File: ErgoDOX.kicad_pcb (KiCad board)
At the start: 2 copper layers, 182.8 x 158.9 mm, 103 parts, among them J1 SPLIT_JACK_TOP, J1 USB, J2 3.5mm, J2 EXT1_TOP, J3 EXT1_BOT, J3 JMP, J4 EXT1_TOP2, J4 JMP, J5 SPLIT_JACK_BOT, J6 USB_C_TOP, J7 USB_C_BOT, SW0:10 SW0:3, SW0:11 SW0:2, SW0:12 SW0:1, SW0:7 SW0:6, SW0:8 SW0:5, SW0:9 SW0:4, SW1:10 SW1:3, SW1:11 SW1:2, SW1:12 SW1:1, SW1:13 SW1:0, SW1:9 SW1:4, SW2:10 SW2:3, SW2:11 SW2:2, SW2:12 SW2:1, SW2:13 SW2:0, SW2:7 SW2:6, SW2:8 SW2:5, SW2:9 SW2:4, SW3:10 SW3:3, SW3:11 SW3:2, SW3:12 SW3:1, SW3:13 SW3:0, SW3:8 SW3:5, SW3:9 SW3:4, SW4:10 SW4:3, SW4:11 SW4:2, SW4:12 SW4:1, SW4:13 SW4:0, SW4:7 SW4:6, SW4:8 SW4:5, SW4:9 SW4:4, SW5:10 SW5:3, SW5:11 SW5:2, SW5:12 SW5:1, SW5:13 SW5:0, SW5:7 SW5:6, SW5:8 SW5:5, SW5:9 SW5:4, U1 STM32F072C8Tx, U1 TEENSY2.0, U2 MCP1700-1202E_SOT23, U2 MCP23018

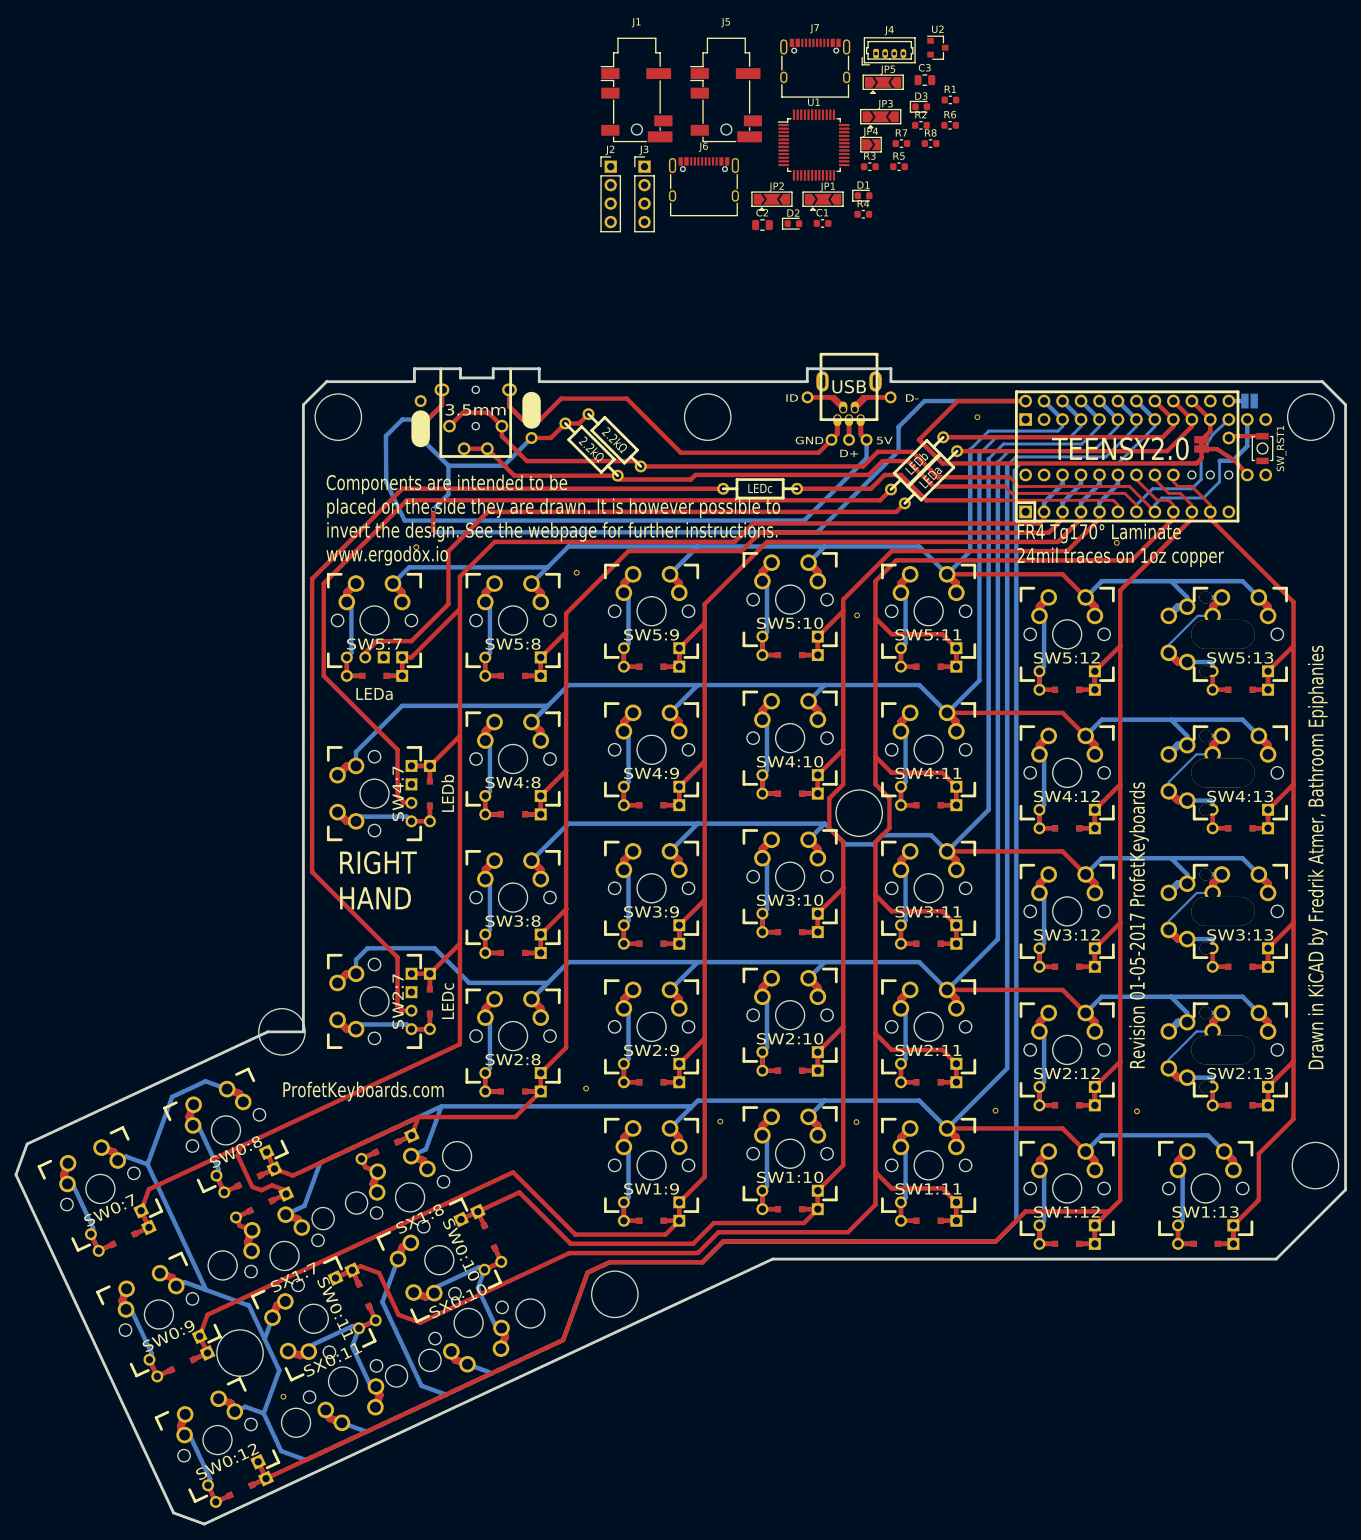
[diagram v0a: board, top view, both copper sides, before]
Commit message: Routing done, needs review.
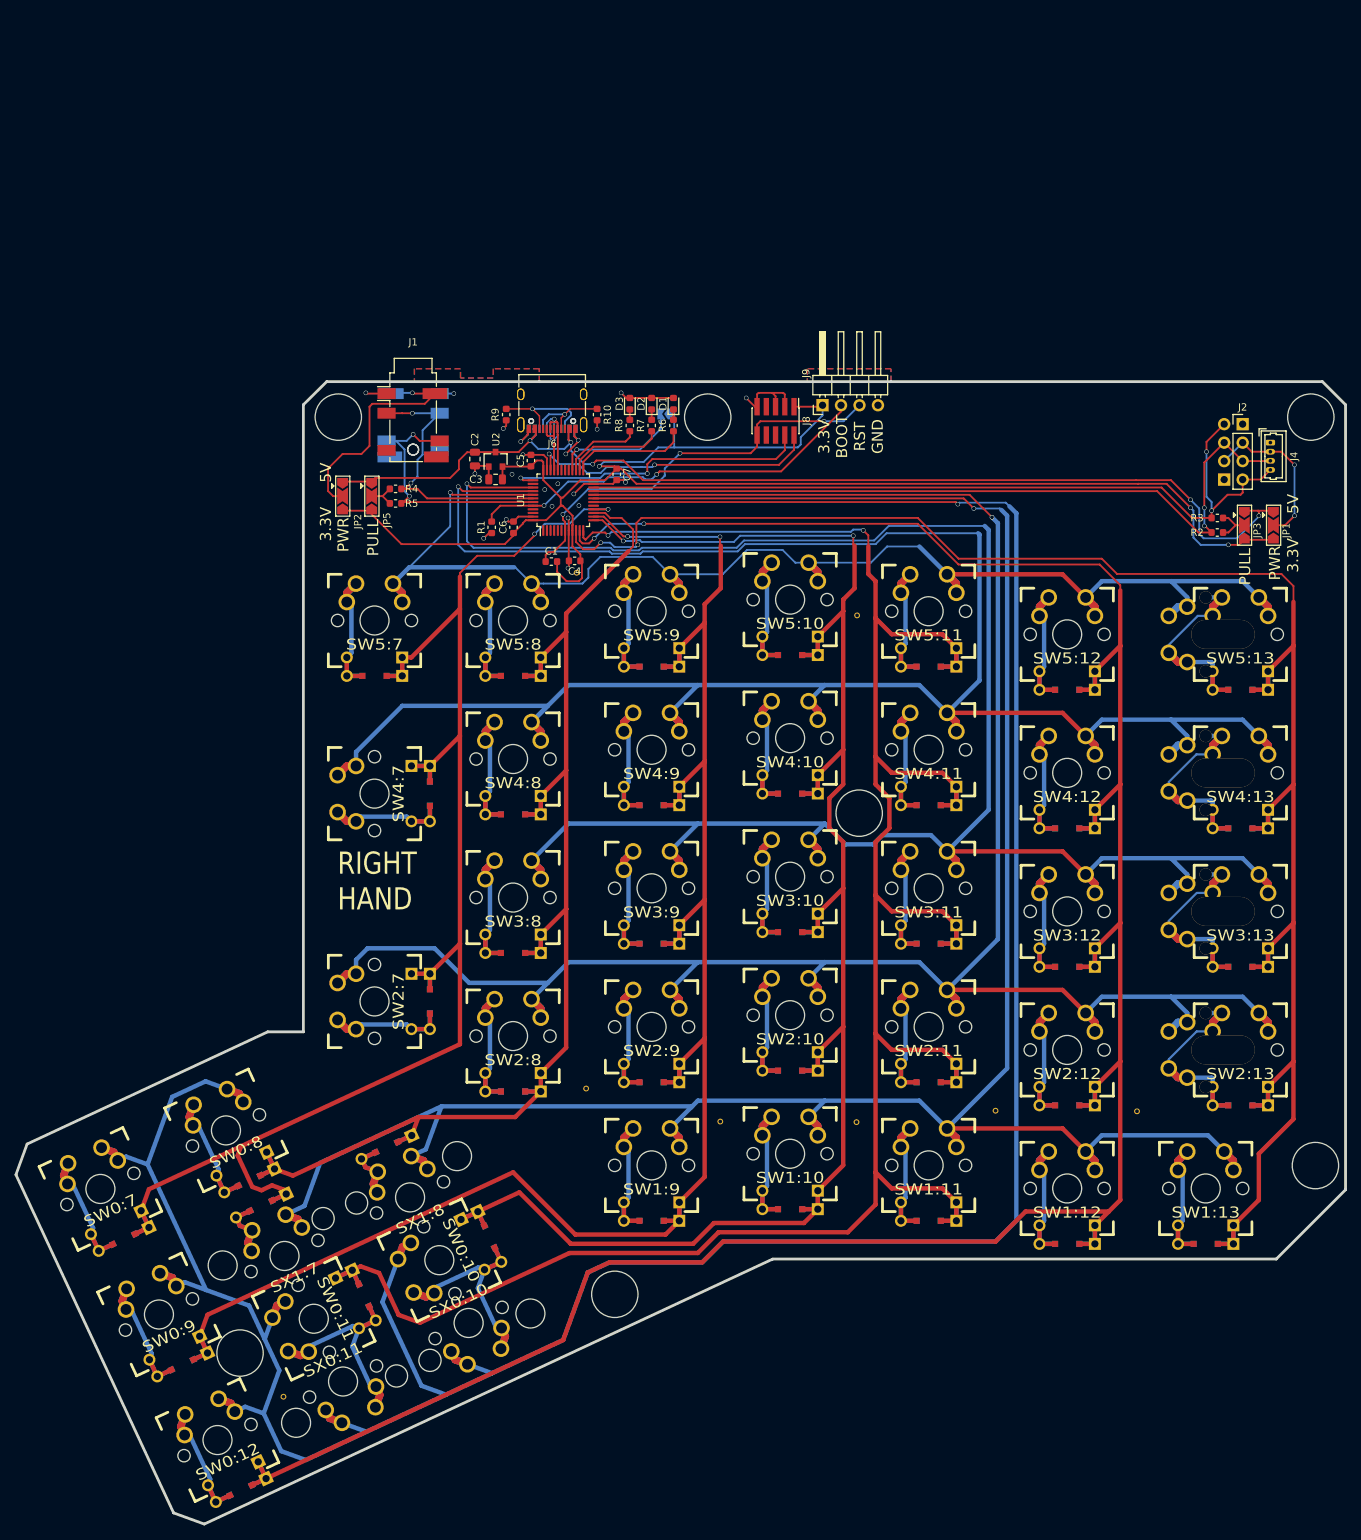
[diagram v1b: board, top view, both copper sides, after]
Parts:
- removed the J1 at (137.6, 30.5)
- removed the J2 at (86.3, 30.5)
- removed the J3 at (94.0, 37.5)
- removed the J4 at (78.7, 37.5)
- removed the JP1 at (186.1, 40.9)
- removed the JP2 at (192.7, 34.9)
- removed LED_A1: LEDa, MX_LED
- removed LED_B1: LEDb, MX_LED
- removed LED_C1: LEDc, MX_LED
- removed the R1 at (105.4, 40.3)
- removed the R2 at (102.2, 41.6)
- removed RA1: LEDa, RESISTOR
- removed RB1: LEDb, RESISTOR
- removed RC1: LEDc, RESISTOR
- removed the STITCHING_VIA at (174.5, 54.4)
- removed the STITCHING_VIA at (78.1, 55.0)
- removed the STITCHING_VIA at (155.3, 37.1)
- removed SW_RST1: SWITCH_PUSH, Buttons_Switches_SMD:SW_SPST_B3U-1000P
- removed the U1 at (175.9, 42.5)
- removed the U2 at (178.4, 41.3)
- added C4: 100n, Capacitor_SMD:C_0603_1608Metric, F.Cu at (99.9, 56.9)
- added C5: 100n, Capacitor_SMD:C_0603_1608Metric, F.Cu at (93.9, 43.1)
- added C6: 100n, Capacitor_SMD:C_0603_1608Metric, F.Cu at (91.5, 52.3)
- added C7: 100n, Capacitor_SMD:C_0603_1608Metric, F.Cu at (105.7, 45.0)
- added J8: Conn_ARM_JTAG_SWD_10, Connector_PinHeader_1.27mm:PinHeader_2x05_P1.27mm_Vertical_SMD, F.Cu at (127.5, 37.6)
- added J9: Conn_01x04, Connector_PinHeader_2.54mm:PinHeader_1x04_P2.54mm_Horizontal, F.Cu at (134.0, 35.5)
- added R10: 5.1k, Resistor_SMD:R_0603_1608Metric, F.Cu at (103.0, 36.8)
- added R9: 5.1k, Resistor_SMD:R_0603_1608Metric, F.Cu at (90.5, 36.8)
- C2, C3: value C -> 1u
- J3, J5, J7, JP4: moved to B.Cu
- moved J2 93.8 mm to (191.8, 38.1)
- moved J3 90.6 mm to (189.2, 45.7)
- moved JP5 90.5 mm to (72.0, 48.0), turned to 270 degrees
- moved R1 86.2 mm to (88.5, 52.3), turned to 90 degrees
- moved R5 83.3 mm to (75.3, 49.0), turned to 180 degrees
- moved U2 83.1 mm to (89.0, 42.9), turned to 90 degrees
- moved C3 80.6 mm to (89.0, 45.7), turned to 180 degrees
- moved JP1 76.4 mm to (196.0, 52.0), turned to 270 degrees
- moved J4 76.2 mm to (195.6, 40.6), turned to 270 degrees
- moved JP3 75.2 mm to (192.0, 52.0), turned to 270 degrees
- moved R4 74.6 mm to (75.3, 47.0), turned to 180 degrees
- moved JP2 71.8 mm to (68.0, 48.0), turned to 270 degrees
- moved R2 69.3 mm to (188.3, 53.0)
- moved R3 67.9 mm to (188.3, 51.0)
- moved J5 61.6 mm to (77.7, 38.2), turned to 180 degrees
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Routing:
- net +3V3: track 0.00 -> 219.6 mm, vias 0 -> 3
- net VCC: track 204.8 -> 0.00 mm, vias 2 -> 0
- net VBUS: track 0.00 -> 153.1 mm, vias 0 -> 5
- net /SDAM: track 128.3 -> 0.00 mm
- net Net-(LED_C1-Pad1): track 127.4 -> 0.00 mm
- net /SCLM: track 119.7 -> 0.00 mm
- net Net-(LED_B1-Pad1): track 119.1 -> 0.00 mm
- net /EXT1_SDA: track 0.00 -> 112.4 mm, vias 0 -> 2
- net /EXT1_SCL: track 0.00 -> 108.7 mm, vias 0 -> 2
- net Net-(J1-Pad1): track 102.6 -> 0.00 mm
- net Net-(LED_A1-Pad1): track 87.6 -> 0.00 mm
- net /COL0: track 159.7 -> 245.3 mm, vias 0 -> 2
- net GND: track 2.22 -> 67.8 mm, vias 0 -> 22
- net /COL6: track 259.5 -> 195.4 mm, vias 0 -> 2
- net Net-(J1-Pad5): track 62.3 -> 0.00 mm
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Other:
- board size 182.8 x 158.9 mm -> 182.8 x 157.1 mm
- net class Default: clearance 0.3048 -> 0.2; trace_width 0.6 -> 0.254
- rule trace_clearance: 0.3048 -> 0.2
- board text added: "3.3V 5V"
- board text added: "3.3V BOOT RST GND"
- board text added: "Ergo72"
- board text added: "Ergo72 by emeryth.net based on ErgoDox by ergodox.io"
- board text added: "PULL"
- board text added: "PWR"
- board text removed: "5V"
- board text removed: "Components are intended to be placed on the side they are drawn. It is however possible to invert the design. See the webpage for further instructions. www.ergodox.io"
- board text removed: "D+"
- board text removed: "D-"
- board text removed: "Design by Dominic Beauchamp, based on the Key64 by Nestor A. Diaz"
- board text removed: "Drawn in KiCAD by Fredrik Atmer, Bathroom Epiphanies"
- board text removed: "ErgoDox"
- board text removed: "FR4 Tg170° Laminate 24mil traces on 1oz copper"
- board text removed: "GND"
- board text removed: "ID"
- board text removed: "ProfetKeyboards.com"
- board text removed: "Revision 01-05-2017 ProfetKeyboards"

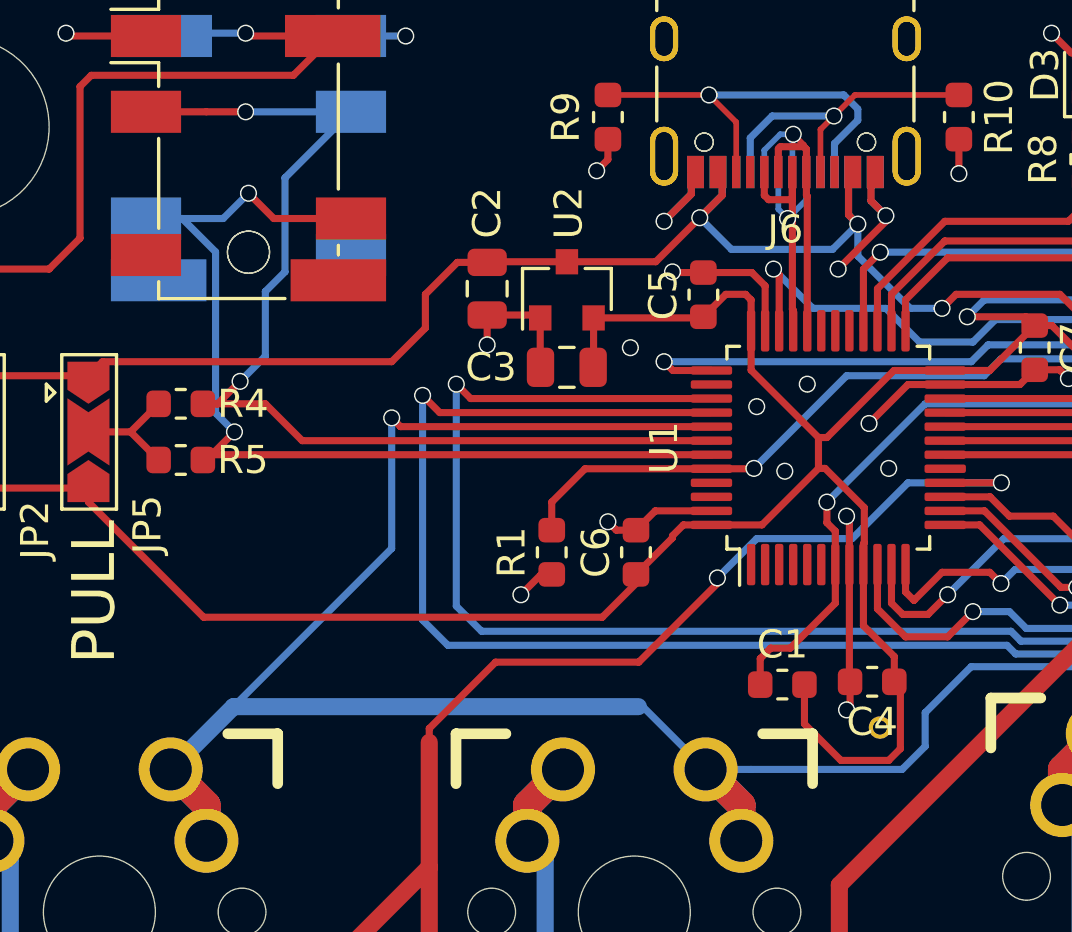
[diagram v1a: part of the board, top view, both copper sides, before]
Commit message: Add testpoints and fix some stuff.
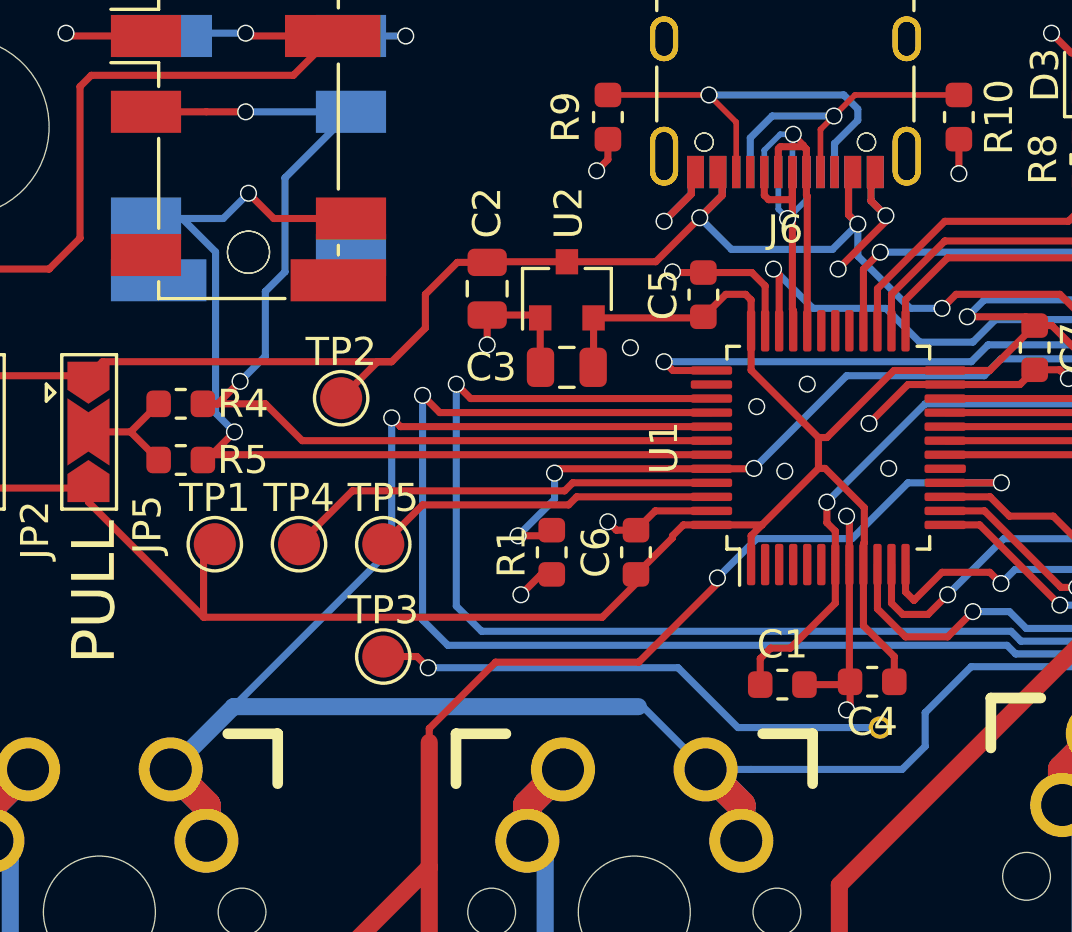
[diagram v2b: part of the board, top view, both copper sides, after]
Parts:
- added TP1: 3V3, TestPoint:TestPoint_Pad_D1.5mm, F.Cu at (76.5, 52.0)
- added TP2: 5V, TestPoint:TestPoint_Pad_D1.5mm, F.Cu at (81.0, 46.8)
- added TP3: GND, TestPoint:TestPoint_Pad_D1.5mm, F.Cu at (82.5, 56.0)
- added TP4: EXT2_SCL, TestPoint:TestPoint_Pad_D1.5mm, F.Cu at (79.5, 52.0)
- added TP5: EXT2_SDA, TestPoint:TestPoint_Pad_D1.5mm, F.Cu at (82.5, 52.0)
- R1: value 1k -> 10k
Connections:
- C1 pad 2: +3V3 -> GND
- U1 pad 1: Net-(U1-Pad1) -> +3V3
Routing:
- net GND: track 67.8 -> 88.8 mm, vias 22 -> 23
- net /EXT2_SCL: track 0.00 -> 15.6 mm
- net /EXT2_SDA: track 0.00 -> 12.4 mm
- net +3V3: track 219.6 -> 216.0 mm
- net VBUS: track 153.1 -> 156.0 mm
- net /BOOT: track 56.0 -> 58.5 mm, vias 2 -> 4
